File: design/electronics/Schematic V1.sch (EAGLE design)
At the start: 160 parts, among them J1 PJ-202AH, J2 PJ-025, U1 STM32F207VGT6TR, U10 SN65LBC175ADD16-M, U11 OPA4205APWRTSSOP14_PW_R-PDSO-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, U12 SN75ALS174ADWRDW20-M, U13 SN75468DRD0016A_M, U14 SN75468DRD0016A_M, U15 ACSL-6400-00TESOIC_6400-00TE-M, U16 ACSL-6400-00TESOIC_6400-00TE-M, U17 SN65LBC175ADD16-M, U18 SN65LBC175ADD16-M, U19 SN65LBC175ADD16-M, U2 LM2678S-5.0/NOPBTS7B-M, U3 VS-6TQ045S-M3DPAK_045S-M3_VIS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, U4 LM2678S-3.3/NOPBTS7B-M, U5 STM32F207VGT6TR, U6 VS-6TQ045S-M3DPAK_045S-M3_VIS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, U7 SN75ALS174ADWRDW20-M, U8 OPA4205APWRTSSOP14_PW_R-PDSO-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, U9 TPS63700DRCR

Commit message: Finished Schematics, Libraries, and BOM
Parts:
- removed R23, R26: 10k, rcl:R-US_R0805
- removed R24, R25: 73k, rcl:R-US_R0805
- removed U11: OPA4205APWRTSSOP14_PW_R-PDSO-G14_TEX-M, SSW-130-01-G-S:OPA4205APWRTSSOP14_PW_R-PDSO-G14_TEX-M
- added C62: 0.1uF, SparkFun-Capacitors:1.0UF-0805-25V-10%
- added J3, J4: DD50P564GTXLF, SSW-130-01-G-S:DD50P564GTXLF
- added J5: SAMTEC-TST-105-01-X-DJ, SSW-130-01-G-S:SAMTEC-TST-105-01-X-DJ
- added J6: SSW-106-02-TM-S-RA, SSW-130-01-G-S:SSW-106-02-TM-S-RA
- added L4: BLM21PG600SN1DIND_BLM21_MUR-M, SSW-130-01-G-S:BLM21PG600SN1DIND_BLM21_MUR-M
- added LED1: BLUE, led:LEDCHIPLED_0805
- added LED2: RED, led:LEDCHIPLED_0805
- added LED3: GREEN, led:LEDCHIPLED_0805
- added LED4: WHITE, led:LEDCHIPLED_0805
- added R69: (no value), rcl:R-US_R0805
- added SW1: TL6330AF200Q, SSW-130-01-G-S:TL6330AF200Q
- added TP1, TP2, TP3, TP4, TP5, TP6: TEST-POINT3X5, SparkFun-Connectors:TEST-POINT3X5
- R10, R12: value 37k -> 73k
- R19: value 10k -> 100
- R20: value 37k -> 680
- R21: value 10k -> 75
- R22: value 37k -> 560
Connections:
- removed net 14V-24V_GND: J1.2, J1.3, J2.2, J2.3, R1.1, U13.E, U14.E
- removed net CLR_EN_GPIO: U12.3/42N, U7.3/42N
- removed net N$21: R19.2, R20.2, U11.-IN_2
- removed net SPEED_ANALOG_1: R12.1, U8.OUT_2
- removed net SPEED_ANALOG_2: R22.1, U11.OUT_2
- removed net SPEED_DAC_1: R11.1
- removed net SPEED_DAC_2: R21.1
- removed net TORQUE_ANALOG_1: R15.1, U8.OUT_4
- removed net TORQUE_ANALOG_2: R25.1, U11.OUT_4
- removed net TORQUE_DAC_1: R16.1
- removed net TORQUE_DAC_2: R26.1
- new net FRWD_EX_TORQUE_LIM_GPIO_1: U1A.PC6
- new net FRWD_EX_TORQUE_LIM_GPIO_2: U1A.PA11
- new net GND: R20.1
- new net N$30: LED4.A, R22.2
- new net NRST: C62.2, J5.1, R69.1, SW1.1, SW1.2, U1B.NRST
- new net SWCLK: J5.6, U1A.PA14
- new net SWDIO: J5.2, U1A.PA13
- new net TORQUE-SPEED_ANALOG_1: J3.5, J3.9, R12.1, U8.OUT_2
- new net TORQUE-SPEED_ANALOG_2: J4.5, J4.9, R15.1, U8.OUT_4
- new net TORQUE-SPEED_DAC_1: R11.1, U1A.PA4
- new net TORQUE-SPEED_DAC_2: R16.1, U1A.PA5
- new net UART_RX: J6.04, U1A.PC11
- new net UART_TX: J6.05, U1A.PC10
- net +14V: now also R22.1, TP4.1
- net +24V: now also J3.47, J4.47
- net +3.3V: now also R21.1, R69.2, TP3.1
- net +5V: now also R19.1, TP1.1
- net -15V: now also LED2.C, TP2.1
- net 1.65V_REF: no longer R19.1, R23.1
- net ABS_ENC_OUT_GPIO_1: now also U1B.PE2
- net ABS_ENC_OUT_GPIO_2: now also U1B.PE6
- net ABS_ENC_OUT_HI_1: now also J3.48
- net ABS_ENC_OUT_HI_2: now also J4.48
- net ABS_ENC_OUT_LO_1: now also J3.49
- net ABS_ENC_OUT_LO_2: now also J4.49
- net ALARM_RST_AN_1: now also J3.44
- net ALARM_RST_AN_2: now also J4.44
- net ALARM_RST_GPIO_1: now also U1A.PD15
- net ALARM_RST_GPIO_2: now also U1A.PA10
- net ALO_AN_A_1: now also J3.37
- net ALO_AN_A_2: now also J4.37
- net ALO_AN_B_1: now also J3.38
- net ALO_AN_B_2: now also J4.38
- net ALO_AN_C_1: now also J3.39
- net ALO_AN_C_2: now also J4.39
- net ALO_GPIO_A_1: now also U1A.PC4
- net ALO_GPIO_A_2: now also U1A.PB0
- net ALO_GPIO_B_1: now also U1A.PC5
- net ALO_GPIO_B_2: now also U1A.PB1
- net ALO_GPIO_C_1: now also U1A.PA7
- net ALO_GPIO_C_2: now also U1A.PB2
- net CLR_GPIO_1: now also U1A.PB14
- net CLR_GPIO_2: now also U1A.PD10
- net CLR_HI_1: now also J3.15
- net CLR_HI_2: now also J4.15
- net CLR_LO_1: now also J3.14
- net CLR_LO_2: now also J4.14
- net DIR_GPIO_1: now also U1A.PB13
- net DIR_GPIO_2: now also U1A.PD9
- net DIR_HI_1: now also J3.11
- net DIR_HI_2: now also J4.11
- net DIR_LO_1: now also J3.12
- net DIR_LO_2: now also J4.12
- net ENC_PUL_OUT_A_GPIO_1: now also U1A.PB9
- net ENC_PUL_OUT_A_GPIO_2: now also U1B.PE3
- net ENC_PUL_OUT_A_HI_1: now also J3.33
- net ENC_PUL_OUT_A_HI_2: now also J4.33
- net ENC_PUL_OUT_A_LO_1: now also J3.34
- net ENC_PUL_OUT_A_LO_2: now also J4.34
- net ENC_PUL_OUT_B_GPIO_1: now also U1B.PE0
- net ENC_PUL_OUT_B_GPIO_2: now also U1B.PE4
- net ENC_PUL_OUT_B_HI_1: now also J3.35
- net ENC_PUL_OUT_B_HI_2: now also J4.35
- net ENC_PUL_OUT_B_LO_1: now also J3.36
- net ENC_PUL_OUT_B_LO_2: now also J4.36
- net ENC_PUL_OUT_C_GPIO_1: now also U1B.PE1
- net ENC_PUL_OUT_C_GPIO_2: now also U1B.PE5
- net ENC_PUL_OUT_C_HI_1: now also J3.19
- net ENC_PUL_OUT_C_HI_2: now also J4.19
- net ENC_PUL_OUT_C_LO_1: now also J3.20
- net ENC_PUL_OUT_C_LO_2: now also J4.20
- net FRWD_DRIVE_EN_AN_1: now also J3.42
- net FRWD_DRIVE_EN_AN_2: now also J4.42
- net FRWD_DRIVE_EN_GPIO_1: now also U1A.PD13
- net FRWD_DRIVE_EN_GPIO_2: now also U1A.PA8
- net FRWD_EX_TORQUE_LIM_EN_AN_1: now also J3.45
- net FRWD_EX_TORQUE_LIM_EN_AN_2: now also J4.45
- net GEN_PURPOSE_OUT_GPIO_A_1: now also U1B.PE8
- net GEN_PURPOSE_OUT_GPIO_A_2: now also U1B.PE12
- net GEN_PURPOSE_OUT_GPIO_B_1: now also U1B.PE9
- net GEN_PURPOSE_OUT_GPIO_B_2: now also U1B.PE13
- net GEN_PURPOSE_OUT_GPIO_C_1: now also U1B.PE10
- net GEN_PURPOSE_OUT_GPIO_C_2: now also U1B.PE14
- net GEN_PURPOSE_OUT_HI_A_1: now also J3.25
- net GEN_PURPOSE_OUT_HI_A_2: now also J4.25
- net GEN_PURPOSE_OUT_HI_B_1: now also J3.27
- net GEN_PURPOSE_OUT_HI_B_2: now also J4.27
- net GEN_PURPOSE_OUT_HI_C_1: now also J3.29
- net GEN_PURPOSE_OUT_HI_C_2: now also J4.29
- net GEN_PURPOSE_OUT_LO_A_1: now also J3.26
- net GEN_PURPOSE_OUT_LO_A_2: now also J4.26
- net GEN_PURPOSE_OUT_LO_B_1: now also J3.28
- net GEN_PURPOSE_OUT_LO_B_2: now also J4.28
- net GEN_PURPOSE_OUT_LO_C_1: now also J3.30
- net GEN_PURPOSE_OUT_LO_C_2: now also J4.30
- net N$22: now also LED1.A, R19.2; no longer R21.2, R22.2, U11.+IN_2
- net N$23: now also LED2.A, R20.2; no longer R23.2, R24.2, U11.-IN_4
- net N$24: now also LED3.A, R21.2; no longer R25.2, R26.2, U11.+IN_4
- net POS_EN_GPIO: now also U1A.PB15
- net PROP_CONTROL_EN_AN_1: now also J3.41
- net PROP_CONTROL_EN_AN_2: now also J4.41
- net PROP_CONTROL_EN_GPIO_1: now also U1A.PD12
- net PROP_CONTROL_EN_GPIO_2: now also U1A.PC9
- net PULSE_GPIO_1: now also U1A.PB12
- net PULSE_GPIO_2: now also U1A.PD8
- net PULSE_HI_1: now also J3.7
- net PULSE_HI_2: now also J4.7
- net PULSE_LO_1: now also J3.8
- net PULSE_LO_2: now also J4.8
- net P_GND: now also J1.2, J1.3, J2.2, J2.3, J3.1, J3.10, J3.6, J4.1, J4.10, J4.6, L4.2, LED1.C, LED3.C, LED4.C, R1.1, TP5.1, U13.E, U14.E; no longer R20.1, R24.1
- net REVERSE_DRIVE_EN_AN_1: now also J3.43
- net REVERSE_DRIVE_EN_AN_2: now also J4.43
- net REVERSE_DRIVE_EN_GPIO_1: now also U1A.PD14
- net REVERSE_DRIVE_EN_GPIO_2: now also U1A.PA9
- net REVERSE_EX_TORQUE_LIM_EN_AN_1: now also J3.46
- net REVERSE_EX_TORQUE_LIM_EN_AN_2: now also J4.46
- net REVERSE_EX_TORQUE_LIM_EN_GPIO_1: now also U1A.PC7
- net REVERSE_EX_TORQUE_LIM_EN_GPIO_2: now also U1A.PA12
- net SERVO_ALARM_OUT_GPIO_1: now also U1B.PE11
- net SERVO_ALARM_OUT_GPIO_2: now also U1B.PE15
- net SERVO_ALARM_OUT_HI_1: now also J3.31
- net SERVO_ALARM_OUT_HI_2: now also J4.31
- net SERVO_ALARM_OUT_LO_1: now also J3.32
- net SERVO_ALARM_OUT_LO_2: now also J4.32
- net SERVO_EN_AN_1: now also J3.40
- net SERVO_EN_AN_2: now also J4.40
- net SERVO_EN_GPIO_1: now also U1A.PD11
- net SERVO_EN_GPIO_2: now also U1A.PC8
- net S_GND: now also C62.1, J5.3, J5.4, J6.01, J6.02, L4.1, SW1.3, SW1.4, TP6.1
- net V_ON: now also U12.3/42N, U7.3/42N
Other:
- note added: "Ground Isolation"
- note added: "Motor 1 Analog Pins"
- note added: "Motor 2 Analog Pins"
- note added: "STLink Connector"
- note added: "STM Reset Button"
- note added: "Test LEDs"
- note added: "UART Connector"
- note added: "Voltage Test Points"

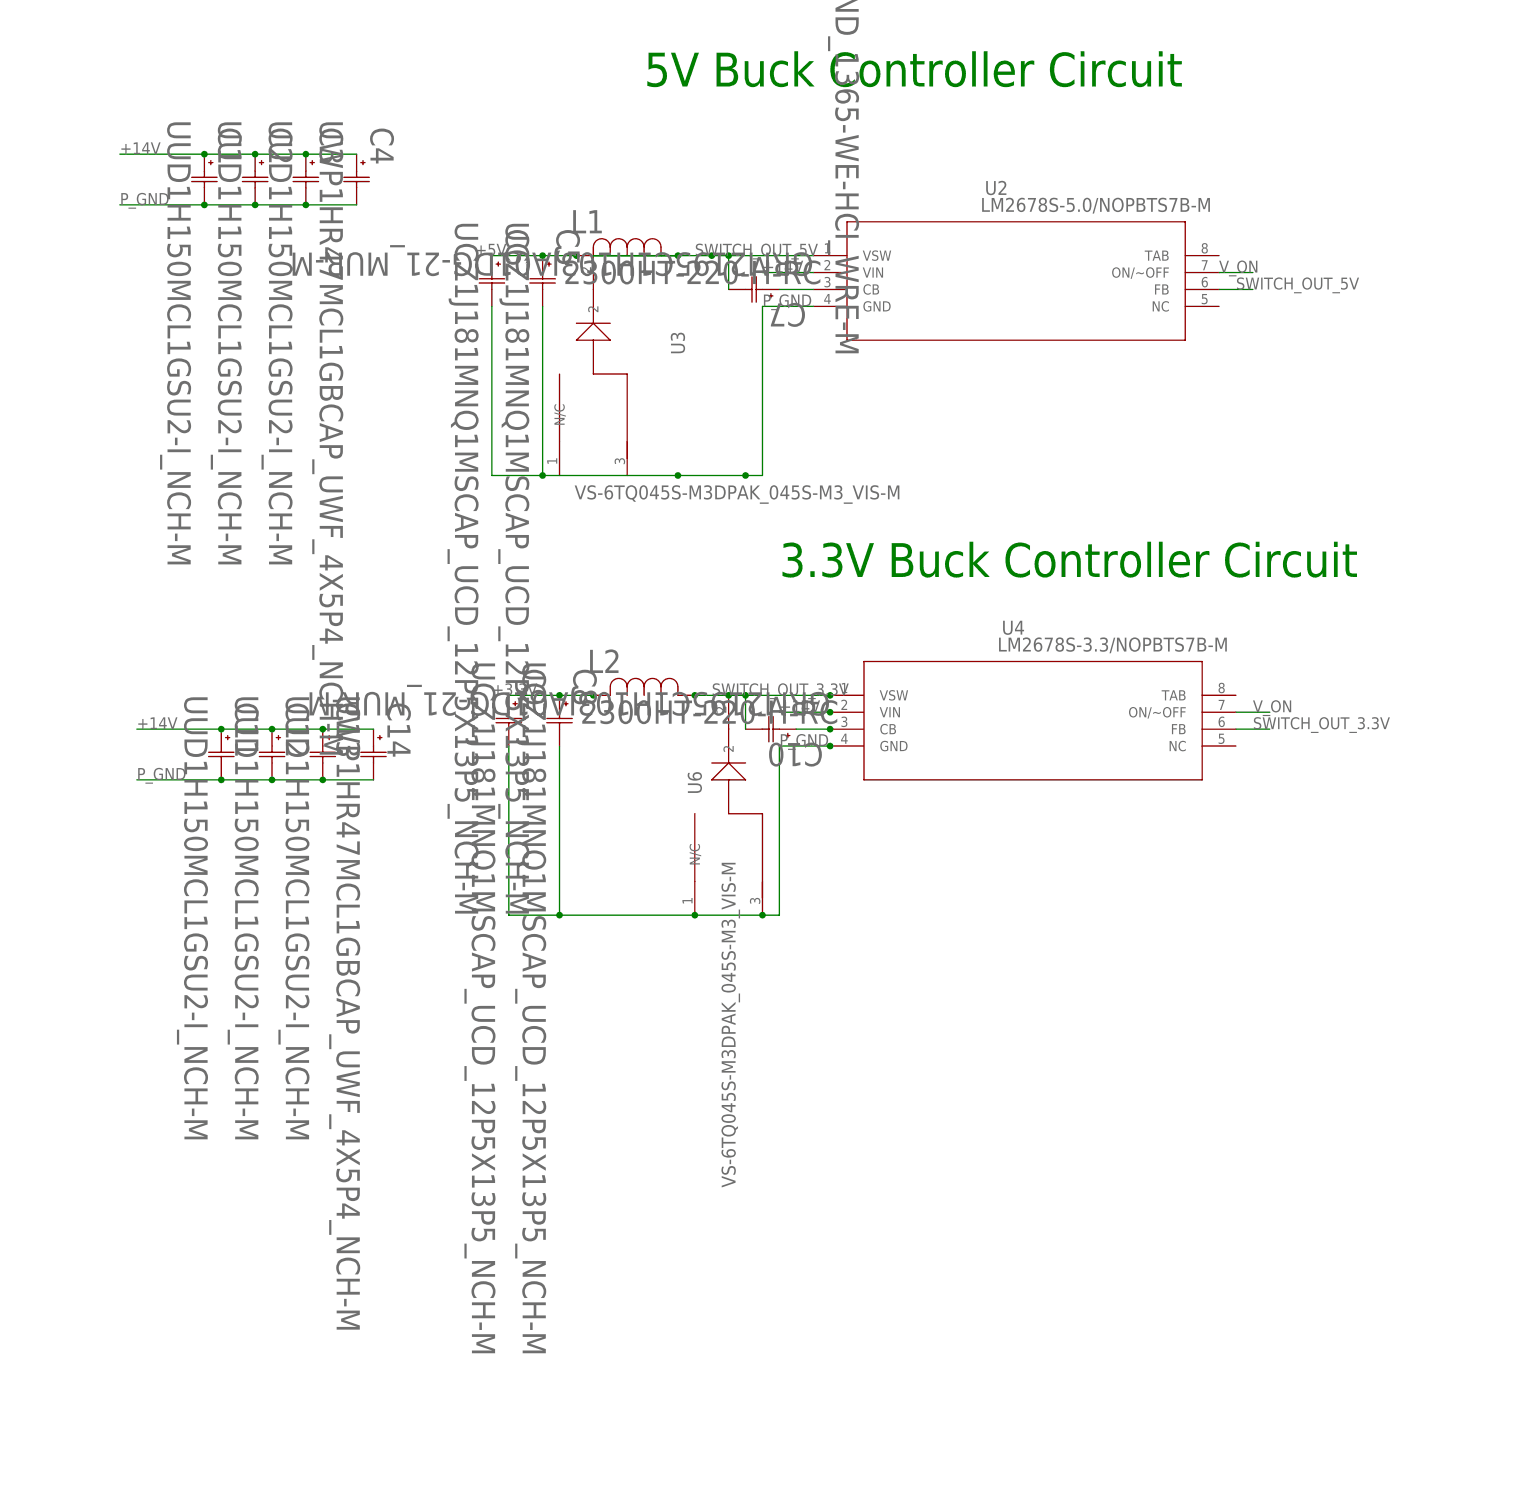
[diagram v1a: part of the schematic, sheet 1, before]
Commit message: Created board layout, updated schematic on Buck Capacitors, Updated BOM, Updated Library
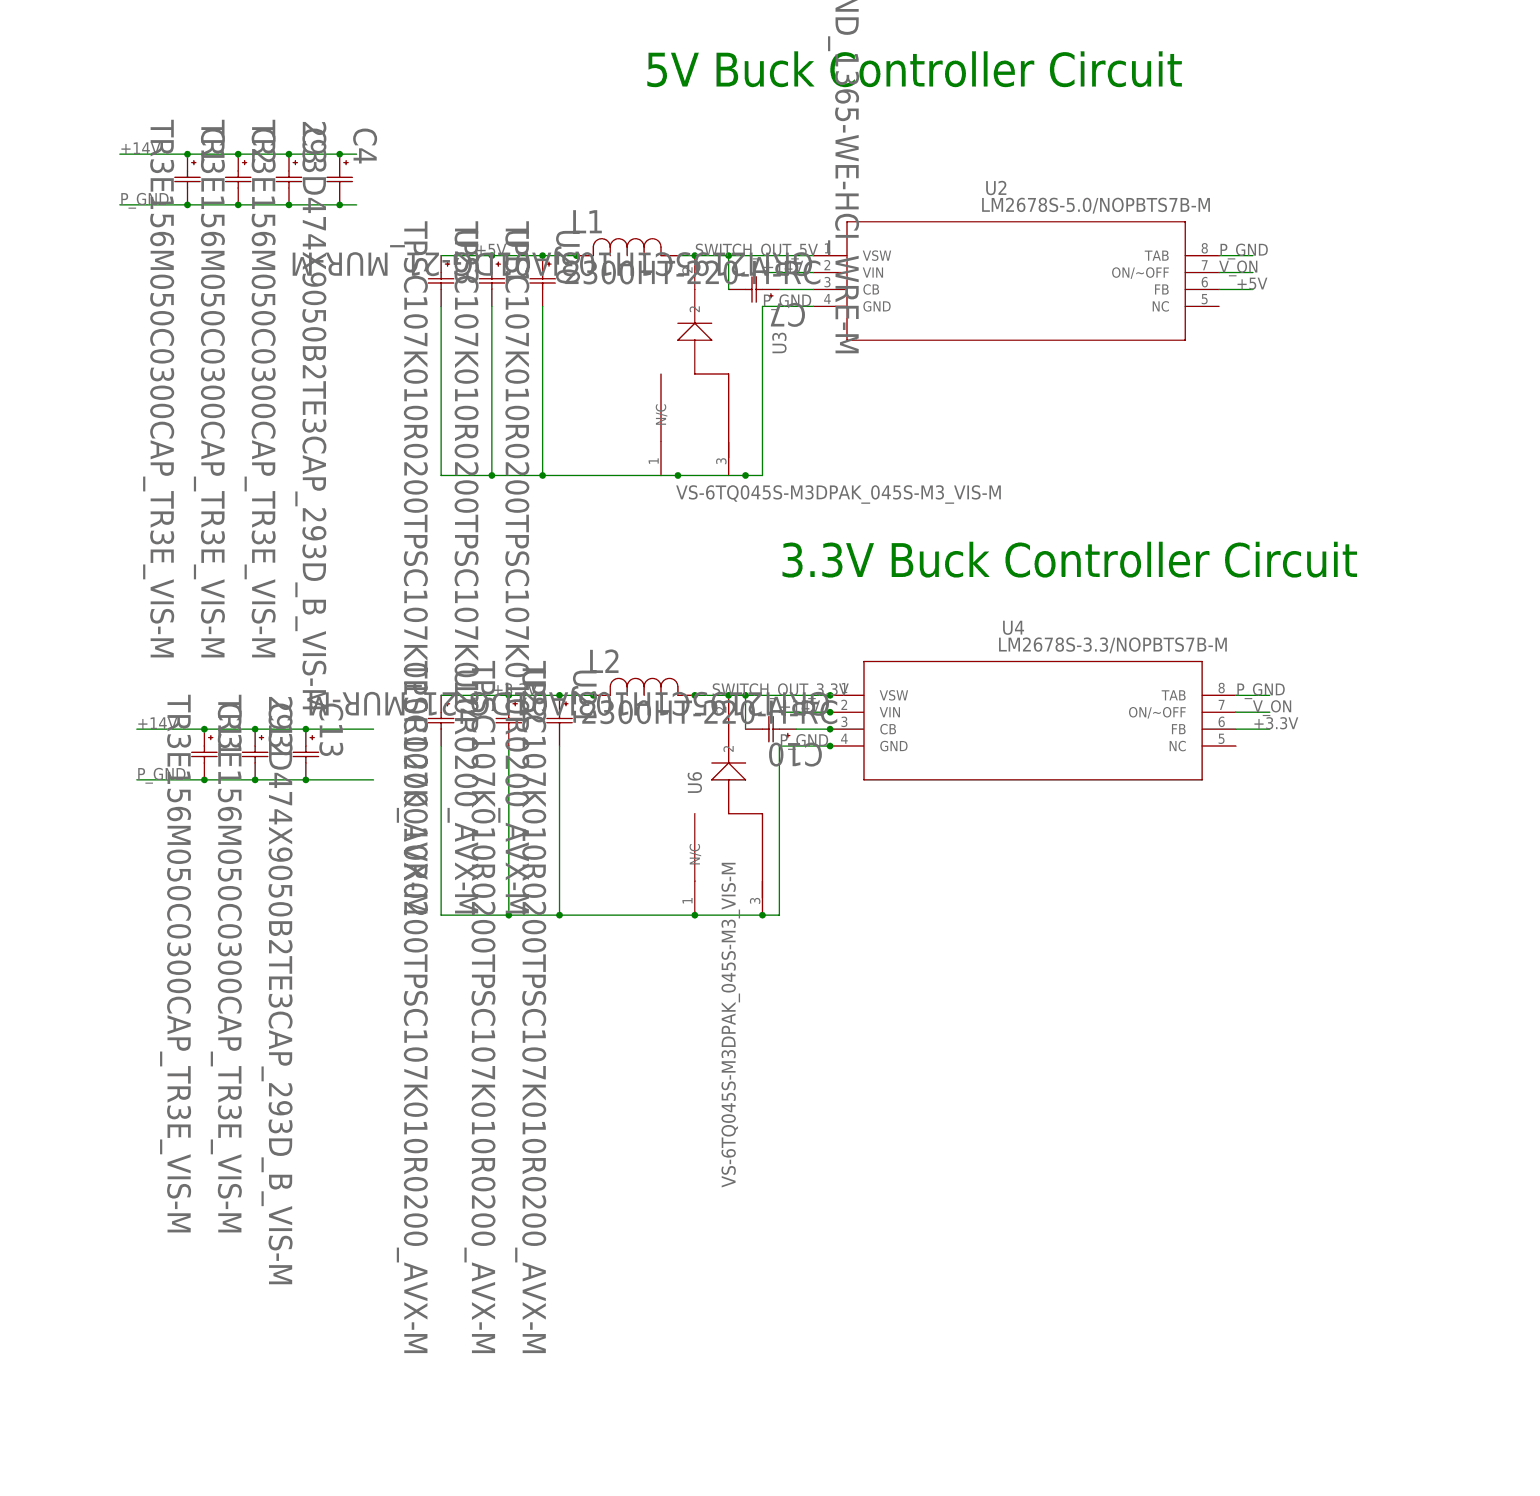
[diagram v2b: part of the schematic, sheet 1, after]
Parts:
- removed C14: UWP1HR47MCL1GBCAP_UWF_4X5P4_NCH-M, SSW-130-01-G-S:UWP1HR47MCL1GBCAP_UWF_4X5P4_NCH-M
- removed C5, C6, C8, C9: UCZ1J181MNQ1MSCAP_UCD_12P5X13P5_NCH-M, SSW-130-01-G-S:UCZ1J181MNQ1MSCAP_UCD_12P5X13P5_NCH-M
- added U11, U20, U21, U22, U23, U24: TPSC107K010R0200TPSC107K010R0200_AVX-M, SSW-130-01-G-S:TPSC107K010R0200TPSC107K010R0200_AVX-M
- C1, C11, C12, C2, C3: value UUD1H150MCL1GSU2-I_NCH-M -> TR3E156M050C0300CAP_TR3E_VIS-M; device SSW-130-01-G-S:UUD1H150MCL1GSU2-I_NCH-M -> SSW-130-01-G-S:TR3E156M050C0300CAP_TR3E_VIS-M
- C13: value UUD1H150MCL1GSU2-I_NCH-M -> 293D474X9050B2TE3CAP_293D_B_VIS-M; device SSW-130-01-G-S:UUD1H150MCL1GSU2-I_NCH-M -> SSW-130-01-G-S:293D474X9050B2TE3CAP_293D_B_VIS-M
- C4: value UWP1HR47MCL1GBCAP_UWF_4X5P4_NCH-M -> 293D474X9050B2TE3CAP_293D_B_VIS-M; device SSW-130-01-G-S:UWP1HR47MCL1GBCAP_UWF_4X5P4_NCH-M -> SSW-130-01-G-S:293D474X9050B2TE3CAP_293D_B_VIS-M
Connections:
- net +14V: no longer C14.1
- net +3.3V: now also U21.4, U22.4, U24.4, U4.FB; no longer C8.1, C9.1
- net +5V: now also U11.4, U2.FB, U20.4, U23.4; no longer C5.1, C6.1
- net P_GND: now also U11.3, U2.TAB, U20.3, U21.3, U22.3, U23.3, U24.3, U4.TAB; no longer C14.2, C5.2, C6.2, C8.2, C9.2
- net SWITCH_OUT_3.3V: no longer U4.FB
- net SWITCH_OUT_5V: no longer U2.FB
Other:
- moved on the sheet: C1, C11, C12, C13, C2, C3, C4, U3

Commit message: Updated Schematic, board layout, BOM, and libraries
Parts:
- removed C10: GRM2195C1H103JA01DG-21_MUR-M, SSW-130-01-G-S:GRM2195C1H103JA01DG-21_MUR-M
- removed C11, C12: TR3E156M050C0300CAP_TR3E_VIS-M, SSW-130-01-G-S:TR3E156M050C0300CAP_TR3E_VIS-M
- removed C13: 293D474X9050B2TE3CAP_293D_B_VIS-M, SSW-130-01-G-S:293D474X9050B2TE3CAP_293D_B_VIS-M
- added C5, C6: 1.0uF, SparkFun-Capacitors:1.0UF-0805-25V-(+80/-20%)
- added H1, H2, H3, H4: MOUNT-HOLE4.1, holes:MOUNT-HOLE4.1
- added L5: BLM21PG600SN1DIND_BLM21_MUR-M, SSW-130-01-G-S:BLM21PG600SN1DIND_BLM21_MUR-M
- L2: value 2300HT-220-H-RC -> BLM21PG600SN1DIND_BLM21_MUR-M; device SSW-130-01-G-S:2300HT-220-H-RC -> SSW-130-01-G-S:BLM21PG600SN1DIND_BLM21_MUR-M
- U21, U22, U24: value TPSC107K010R0200TPSC107K010R0200_AVX-M -> RS0104YQTSSOP-14_JRT-M; device SSW-130-01-G-S:TPSC107K010R0200TPSC107K010R0200_AVX-M -> SSW-130-01-G-S:RS0104YQTSSOP-14_JRT-M
- U4: value LM2678S-3.3/NOPBTS7B-M -> TLV1117LV33DCYR; device SSW-130-01-G-S:LM2678S-3.3/NOPBTS7B-M -> SSW-130-01-G-S:TLV1117LV33DCYR
- U6: value VS-6TQ045S-M3DPAK_045S-M3_VIS-M -> RS0104YQTSSOP-14_JRT-M; device SSW-130-01-G-S:VS-6TQ045S-M3DPAK_045S-M3_VIS-M -> SSW-130-01-G-S:RS0104YQTSSOP-14_JRT-M
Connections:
- removed net N$1: C10.1, U4.CB
- removed net SWITCH_OUT_3.3V: C10.2, L2.1, U4.VSW, U6.2
- new net ABS_ENC_OUT_GPIO_1_5V: U10.4Y, U21.A4
- new net ABS_ENC_OUT_GPIO_2_5V: U17.4Y, U24.A4
- new net ENC_PUL_OUT_A_GPIO_1_5V: U10.1Y, U21.A1
- new net ENC_PUL_OUT_A_GPIO_2_5V: U17.1Y, U24.A1
- new net ENC_PUL_OUT_B_GPIO_1_5V: U10.2Y, U21.A2
- new net ENC_PUL_OUT_B_GPIO_2_5V: U17.2Y, U24.A2
- new net ENC_PUL_OUT_C_GPIO_1_5V: U10.3Y, U21.A3
- new net ENC_PUL_OUT_C_GPIO_2_5V: U17.3Y, U24.A3
- new net GEN_PURPOSE_OUT_GPIO_A_1_5V: U18.1Y, U22.A1
- new net GEN_PURPOSE_OUT_GPIO_A_2_5V: U6.A1
- new net GEN_PURPOSE_OUT_GPIO_B_1_5V: U18.2Y, U22.A2
- new net GEN_PURPOSE_OUT_GPIO_B_2_5V: U6.A2
- new net GEN_PURPOSE_OUT_GPIO_C_1_5V: U18.3Y, U22.A3
- new net GEN_PURPOSE_OUT_GPIO_C_2_5V: U6.A3
- new net N$14: C32.2, C33.2, L5.1, U5C.VDDA
- new net SERVO_ALARM_OUT_GPIO_1_5V: U18.4Y, U22.A4
- new net SERVO_ALARM_OUT_GPIO_2_5V: U6.A4
- new net S_GNDA: L2.2, U5C.VSSA
- net +14V: no longer C11.1, C12.1, C13.1, U4.VIN
- net +3.3V: now also C6.1, L5.2, U21.VCCB, U22.VCCB, U24.VCCB, U4.OUT_2, U4.OUT_4, U6.VCCB; no longer C32.2, C33.2, L2.2, U21.4, U22.4, U24.4, U4.FB, U5C.VDDA
- net +5V: now also C5.1, U21.OE, U21.VCCA, U22.OE, U22.VCCA, U24.OE, U24.VCCA, U4.IN, U6.OE, U6.VCCA
- net ABS_ENC_OUT_GPIO_1: now also U21.B4; no longer U10.4Y
- net ABS_ENC_OUT_GPIO_2: now also U24.B4; no longer U17.4Y
- net ENC_PUL_OUT_A_GPIO_1: now also U21.B1; no longer U10.1Y
- net ENC_PUL_OUT_A_GPIO_2: now also U24.B1; no longer U17.1Y
- net ENC_PUL_OUT_B_GPIO_1: now also U21.B2; no longer U10.2Y
- net ENC_PUL_OUT_B_GPIO_2: now also U24.B2; no longer U17.2Y
- net ENC_PUL_OUT_C_GPIO_1: now also U21.B3; no longer U10.3Y
- net ENC_PUL_OUT_C_GPIO_2: now also U24.B3; no longer U17.3Y
- net GEN_PURPOSE_OUT_GPIO_A_1: now also U22.B1; no longer U18.1Y
- net GEN_PURPOSE_OUT_GPIO_A_2: now also U6.B1
- net GEN_PURPOSE_OUT_GPIO_B_1: now also U22.B2; no longer U18.2Y
- net GEN_PURPOSE_OUT_GPIO_B_2: now also U6.B2
- net GEN_PURPOSE_OUT_GPIO_C_1: now also U22.B3; no longer U18.3Y
- net GEN_PURPOSE_OUT_GPIO_C_2: now also U6.B3
- net P_GND: now also C5.2, C6.2; no longer C11.2, C12.2, C13.2, U21.3, U22.3, U24.3, U4.TAB, U6.ANODE, U6.N/C
- net SERVO_ALARM_OUT_GPIO_1: now also U22.B4; no longer U18.4Y
- net SERVO_ALARM_OUT_GPIO_2: now also U6.B4
- net S_GND: now also L2.1, U21.GND, U22.GND, U24.GND, U6.GND; no longer U5C.VSSA
- net V_ON: no longer U4.ON/~OFF
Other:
- note added: "3.3V LDO Circuit"
- note added: "Level Shifter for Receiver ICs'"
- note added: "Mounting Holes"
- note removed: "3.3V Buck Controller Circuit"
- moved on the sheet: C60, C61, D1, D2, D3, D4, D5, D6, L2, R17, R18, R27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

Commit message: Updated layout parts
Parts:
- removed U20, U23: TPSC107K010R0200TPSC107K010R0200_AVX-M, SSW-130-01-G-S:TPSC107K010R0200TPSC107K010R0200_AVX-M
- C1: value TR3E156M050C0300CAP_TR3E_VIS-M -> 0.1uF; device SSW-130-01-G-S:TR3E156M050C0300CAP_TR3E_VIS-M -> SparkFun-Capacitors:1.0UF-0805-25V-(+80/-20%)
- C2: value TR3E156M050C0300CAP_TR3E_VIS-M -> 20SVPF180MPCAP_SVP_E7_PAN-M; device SSW-130-01-G-S:TR3E156M050C0300CAP_TR3E_VIS-M -> SSW-130-01-G-S:20SVPF180MPCAP_SVP_E7_PAN-M
- C3: value TR3E156M050C0300CAP_TR3E_VIS-M -> 10SVPC330MCAP_SVPC_E7_PAN-M; device SSW-130-01-G-S:TR3E156M050C0300CAP_TR3E_VIS-M -> SSW-130-01-G-S:10SVPC330MCAP_SVPC_E7_PAN-M
- C4: value 293D474X9050B2TE3CAP_293D_B_VIS-M -> 10pF; device SSW-130-01-G-S:293D474X9050B2TE3CAP_293D_B_VIS-M -> SparkFun-Capacitors:10UF-0805-25V-10%
- L1: value 2300HT-220-H-RC -> SRP1270-100MIND_BOURNS_SRP1270-M; device SSW-130-01-G-S:2300HT-220-H-RC -> SSW-130-01-G-S:SRP1270-100MIND_BOURNS_SRP1270-M
- U11: value TPSC107K010R0200TPSC107K010R0200_AVX-M -> MAX7375AXR805+T21-0075D_MXM-M; device SSW-130-01-G-S:TPSC107K010R0200TPSC107K010R0200_AVX-M -> SSW-130-01-G-S:MAX7375AXR805+T21-0075D_MXM-M
- U3: value VS-6TQ045S-M3DPAK_045S-M3_VIS-M -> CDBC520-GCDBC-G-M; device SSW-130-01-G-S:VS-6TQ045S-M3DPAK_045S-M3_VIS-M -> SSW-130-01-G-S:CDBC520-GCDBC-G-M
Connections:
- new net EXT_CLK: U11.CLOCK
- new net N$1: U1B.PH0/OSC_IN
- net +14V: now also C1.2; no longer C1.1, C3.1, C4.1
- net +3.3V: now also C4.2, U11.V+
- net +5V: now also C3.1; no longer U11.4, U20.4, U23.4
- net P_GND: now also C1.1, U3.2; no longer C1.2, C4.2, U11.3, U20.3, U23.3, U3.ANODE, U3.N/C
- net SWITCH_OUT_5V: now also U3.1; no longer U3.2
- net S_GND: now also C4.1, U11.GND
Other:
- moved on the sheet: C3, C62, H1, H2, H3, H4, J5, J6, R69, SW1
